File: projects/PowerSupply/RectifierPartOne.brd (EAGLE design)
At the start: 100 x 80 mm, 27 parts, among them K1 G2R2, K2 G2R2, X1 LINE-IN, X2 T1-PRI, X3 T1-SEC, X4 R1-OUT, X5 T2-PRI, X6 T2-SEC, X7 R2-OUT

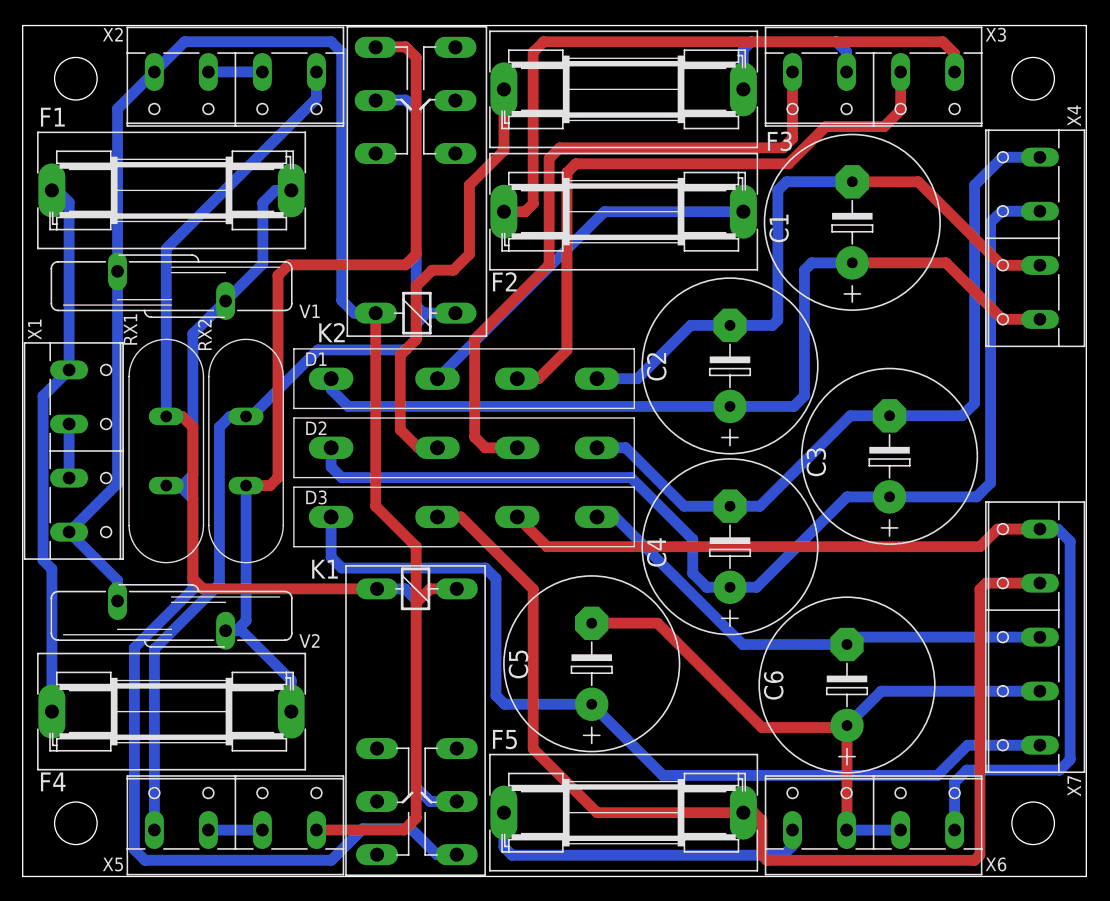
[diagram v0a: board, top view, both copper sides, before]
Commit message: feat: rectifier part modified
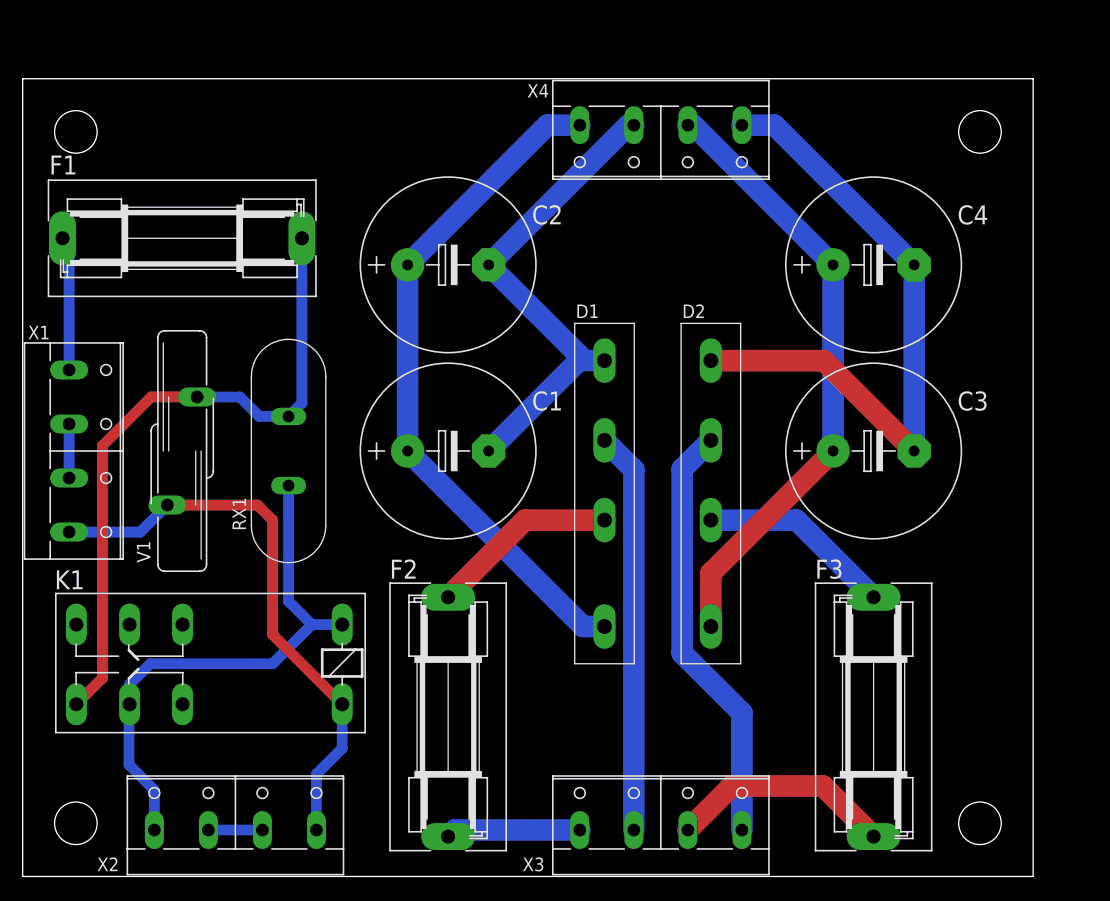
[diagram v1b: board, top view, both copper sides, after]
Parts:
- removed C5, C6: 2200µF, rcl:E7,5-16
- removed D3: B40C5000-3300A, bb84:B..C
- removed F4: 1.6AT, fuse:SH22,5A
- removed F5: 12AT, fuse:SH22,5A
- removed K2: G2R2, relay:G2R2
- removed RX2: B57364-S259, bb84:B57364S0
- removed V2: S20K230, varistor:S20K230
- removed X5: T2-PRI, con-wago-508:W237-4P
- removed X6: T2-SEC, con-wago-508:W237-4P
- removed X7: R2-OUT, con-wago-508:W237-5P
- moved X3 72.8 mm to (60.0, 5.00), turned to 0 degrees
- moved X2 70.0 mm to (20.0, 5.00), turned to 0 degrees
- moved F3 63.5 mm to (80.0, 15.0), turned to 90 degrees
- moved F2 50.3 mm to (40.0, 15.0), turned to 90 degrees
- moved D2 45.5 mm to (67.5, 20.0), turned to 90 degrees
- moved C1 43.7 mm to (40.0, 40.0), turned to 0 degrees
- moved D1 40.0 mm to (57.5, 20.0), turned to 90 degrees
- moved X4 36.4 mm to (60.0, 70.0), turned to 180 degrees
- moved C4 29.7 mm to (80.0, 57.5), turned to 0 degrees
- moved C2 28.2 mm to (40.0, 57.5), turned to 0 degrees
- moved V1 15.5 mm to (15.0, 40.0), turned to 0 degrees
- moved RX1 11.5 mm to (25.0, 40.0), turned to 90 degrees
- moved K1 10.5 mm to (27.5, 20.0), turned to 180 degrees
- moved F1 4.61 mm to (15.0, 60.0)
- moved C3 1.58 mm to (80.0, 40.0), turned to 0 degrees
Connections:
- removed net N$11: F4.2, K2.S1, RX2.P$2, V2.2
- removed net N$17: F5.1, X6.1
- removed net N$18: D3.VAC1, F5.2, X7.4
- removed net N$19: D3.VAC2, X6.4, X7.5
- removed net N$20: C5.+, D3.+VDC, X7.1
- removed net N$21: C6.-, D3.-VDC, X7.3
- removed net N$22: C5.-, C6.+, X6.2, X6.3, X7.2
- removed net N$23: X5.2, X5.3
- removed net N$24: K2.1, K2.P1, RX2.P$1, X5.1
- net +230VAC: no longer F4.1
- net -230VAC: no longer K2.2, V2.1, X5.4
- net N$4: now also X4.4; no longer X4.1
- net N$6: now also X4.2; no longer X4.3
- net N$7: now also X4.3; no longer X4.2
- net N$9: now also X4.1; no longer X4.4
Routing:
- net -230VAC: track 164.4 -> 53.6 mm
- net N$18: track 106.1 -> 0.00 mm
- net N$24: track 91.8 -> 0.00 mm
- net N$19: track 91.1 -> 0.00 mm
- net N$20: track 86.5 -> 0.00 mm
- net N$11: track 84.9 -> 0.00 mm
- net N$22: track 62.5 -> 0.00 mm
- net N$2: track 99.2 -> 51.0 mm
- net N$21: track 46.9 -> 0.00 mm
- net N$8: track 59.5 -> 12.6 mm
- net N$6: track 104.0 -> 57.9 mm
- net N$3: track 105.6 -> 62.8 mm
- net +230VAC: track 51.3 -> 12.6 mm
- net N$17: track 32.5 -> 0.00 mm
- net N$15: track 63.4 -> 40.1 mm
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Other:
- board size 100 x 80 mm -> 95 x 75 mm

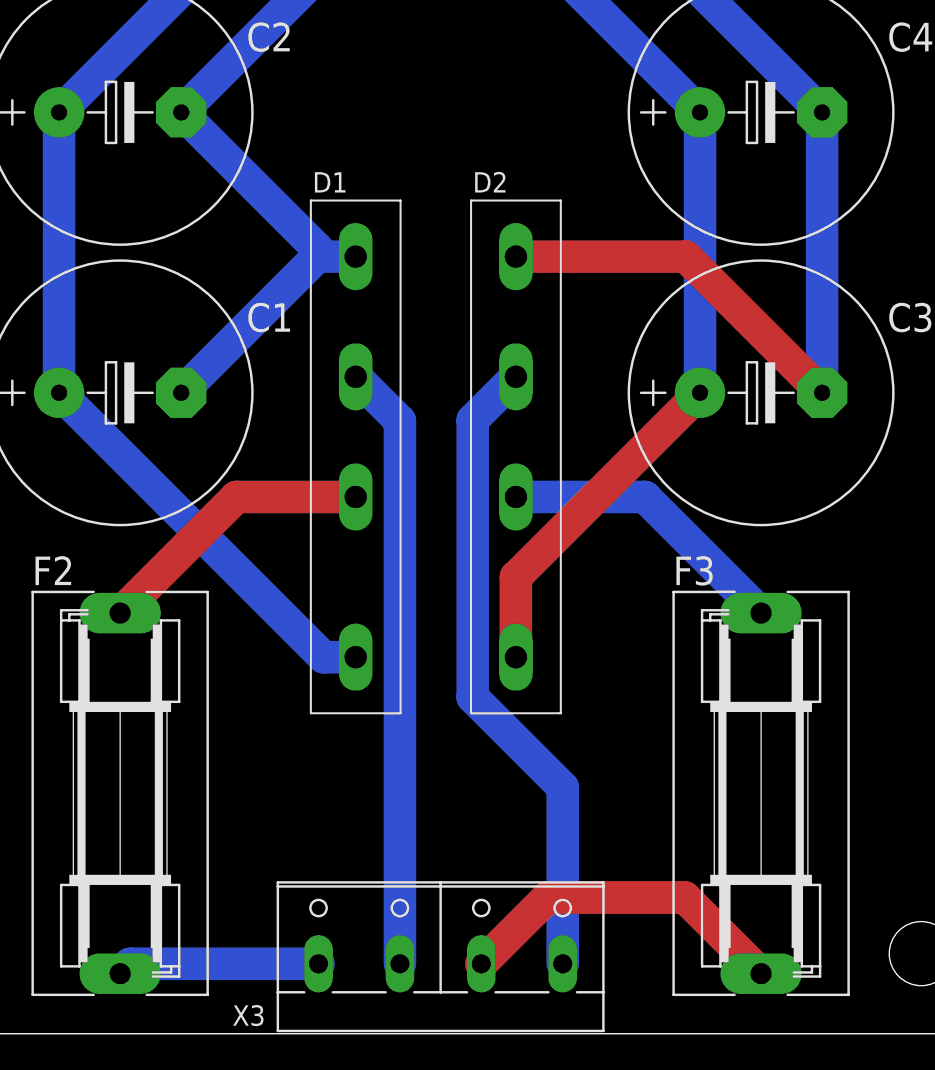
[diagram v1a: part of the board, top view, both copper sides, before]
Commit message: feat: rectifier part one modified
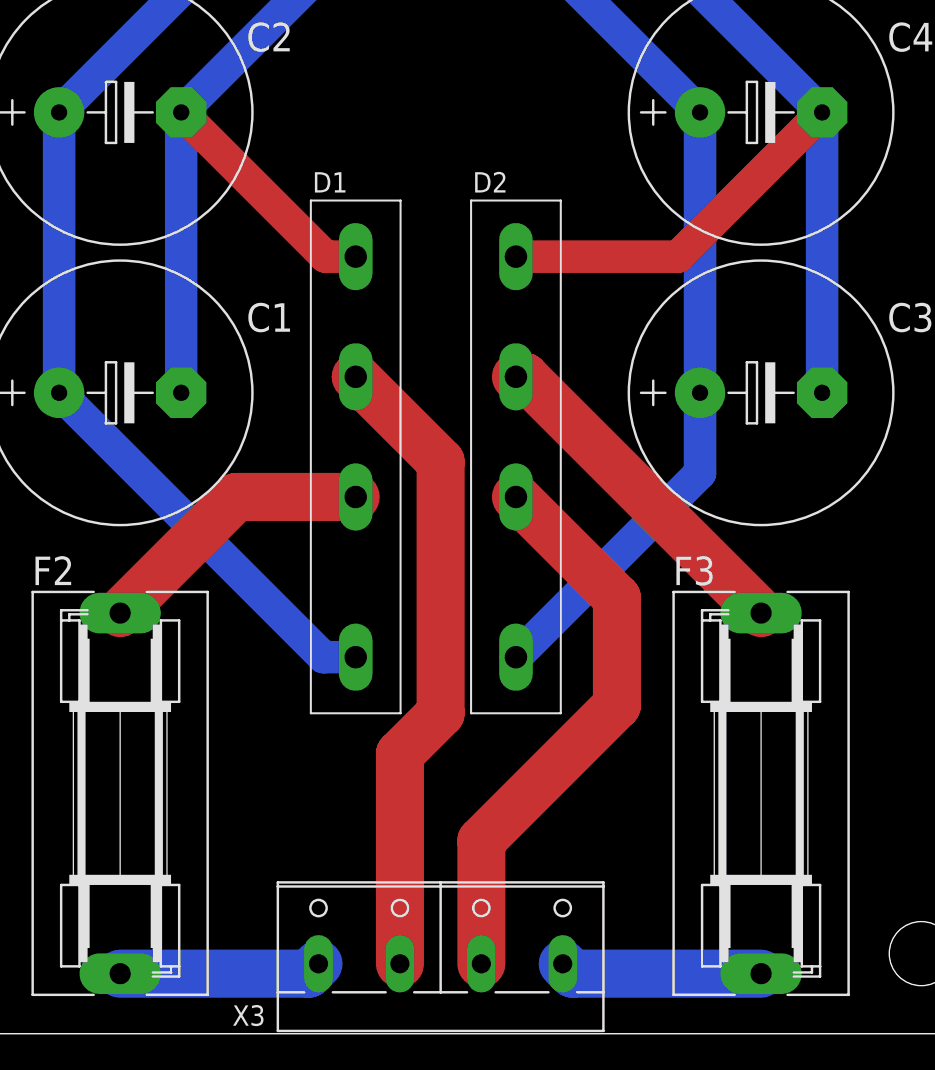
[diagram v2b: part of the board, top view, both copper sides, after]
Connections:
- removed net N$13: F3.1, X3.3
- removed net N$15: D2.VAC2, X3.4
- new net N$11: D2.VAC2, F3.2
- new net N$12: F3.1, X3.4
- net N$14: now also X3.3; no longer F3.2
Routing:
- net N$15: track 40.1 -> 0.00 mm
- net N$11: track 0.00 -> 21.4 mm
- net N$13: track 21.1 -> 0.00 mm
- net N$14: track 18.3 -> 35.2 mm
- net N$12: track 0.00 -> 12.6 mm
- net N$7: track 46.0 -> 51.2 mm
- net N$1: track 37.8 -> 39.9 mm
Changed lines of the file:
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@@
 <contactref element="C1" pad="+"/>
 <contactref element="X4" pad="4"/>
-<wire x1="36.19" y1="57.5" x2="49.325" y2="70.635" width="2.032" layer="16"/>
-<wire x1="49.325" y1="70.635" x2="52.38" y2="70.635" width="2.032" layer="16"/>
 <wire x1="54.7" y1="23.5" x2="52.69" y2="23.5" width="2.032" layer="16"/>
 <wire x1="52.69" y1="23.5" x2="36.19" y2="40" width="2.032" layer="16"/>
 <wire x1="36.19" y1="40" x2="36.19" y2="57.5" width="2.032" layer="16"/>
+<wire x1="36.19" y1="57.5" x2="49.325" y2="70.635" width="2.032" layer="16"/>
+<wire x1="49.325" y1="70.635" x2="52.38" y2="70.635" width="2.032" layer="16"/>
 </signal>
 <signal name="N$6">
@@
 <wire x1="76.19" y1="57.5" x2="63.055" y2="70.635" width="2.032" layer="16"/>
 <wire x1="63.055" y1="70.635" x2="62.54" y2="70.635" width="2.032" layer="16"/>
-<wire x1="64.7" y1="23.5" x2="64.7" y2="28.51" width="2.032" layer="1"/>
-<wire x1="64.7" y1="28.51" x2="76.19" y2="40" width="2.032" layer="1"/>
+<wire x1="76.19" y1="40" x2="76.19" y2="34.99" width="2.032" layer="16"/>
+<wire x1="76.19" y1="34.99" x2="64.7" y2="23.5" width="2.032" layer="16"/>
 </signal>
 <signal name="N$7">
@@
 <contactref element="C2" pad="-"/>
 <contactref element="X4" pad="3"/>
-<wire x1="43.81" y1="40" x2="52.31" y2="48.5" width="2.032" layer="16"/>
-<wire x1="52.31" y1="48.5" x2="54.7" y2="48.5" width="2.032" layer="16"/>
-<wire x1="52.31" y1="48.5" x2="52.31" y2="49" width="2.032" layer="16"/>
-<wire x1="52.31" y1="49" x2="43.81" y2="57.5" width="2.032" layer="16"/>
 <wire x1="43.81" y1="57.5" x2="56.945" y2="70.635" width="2.032" layer="16"/>
 <wire x1="56.945" y1="70.635" x2="57.46" y2="70.635" width="2.032" layer="16"/>
+<wire x1="43.81" y1="57.5" x2="43.81" y2="40" width="2.032" layer="16"/>
+<wire x1="54.7" y1="48.5" x2="52.81" y2="48.5" width="2.032" layer="1"/>
+<wire x1="52.81" y1="48.5" x2="43.81" y2="57.5" width="2.032" layer="1"/>
 </signal>
 <signal name="N$9">
@@
 <wire x1="70.675" y1="70.635" x2="67.62" y2="70.635" width="2.032" layer="16"/>
 <wire x1="83.81" y1="57.5" x2="83.81" y2="40" width="2.032" layer="16"/>
-<wire x1="64.7" y1="48.5" x2="75.31" y2="48.5" width="2.032" layer="1"/>
-<wire x1="75.31" y1="48.5" x2="83.81" y2="40" width="2.032" layer="1"/>
+<wire x1="64.7" y1="48.5" x2="74.81" y2="48.5" width="2.032" layer="1"/>
+<wire x1="74.81" y1="48.5" x2="83.81" y2="57.5" width="2.032" layer="1"/>
 </signal>
 <signal name="PE">
@@
 <contactref element="D1" pad="VAC2"/>
 <contactref element="X3" pad="2"/>
-<wire x1="57.46" y1="4.365" x2="57.46" y2="38.24" width="2.032" layer="16"/>
-<wire x1="57.46" y1="38.24" x2="54.7" y2="41" width="2.032" layer="16"/>
+<wire x1="57.46" y1="4.365" x2="57.46" y2="17.46" width="3" layer="1"/>
+<wire x1="57.46" y1="17.46" x2="60" y2="20" width="3" layer="1"/>
+<wire x1="60" y1="20" x2="60" y2="35.7" width="3" layer="1"/>
+<wire x1="60" y1="35.7" x2="54.7" y2="41" width="3" layer="1"/>
 </signal>
 <signal name="N$8">
 <contactref element="X3" pad="1"/>
 <contactref element="F2" pad="1"/>
-<wire x1="52.38" y1="4.365" x2="40.6172" y2="4.365" width="2.032" layer="16"/>
-<wire x1="40.6172" y1="4.365" x2="40" y2="3.7478" width="2.032" layer="16"/>
+<wire x1="40" y1="3.7478" x2="51.7628" y2="3.7478" width="3" layer="16"/>
+<wire x1="51.7628" y1="3.7478" x2="52.38" y2="4.365" width="3" layer="16"/>
 </signal>
 <signal name="N$10">
 <contactref element="F2" pad="2"/>
 <contactref element="D1" pad="VAC1"/>
-<wire x1="40" y1="26.2522" x2="47.2478" y2="33.5" width="2.032" layer="1"/>
-<wire x1="47.2478" y1="33.5" x2="54.7" y2="33.5" width="2.032" layer="1"/>
-</signal>
-<signal name="N$13">
-<contactref element="X3" pad="3"/>
-<contactref element="F3" pad="1"/>
-<wire x1="62.54" y1="4.365" x2="66.675" y2="8.5" width="2.032" layer="1"/>
-<wire x1="75.2478" y1="8.5" x2="80" y2="3.7478" width="2.032" layer="1"/>
-<wire x1="66.675" y1="8.5" x2="75.2478" y2="8.5" width="2.032" layer="1"/>
+<wire x1="40" y1="26.2522" x2="47.2478" y2="33.5" width="3" layer="1"/>
+<wire x1="47.2478" y1="33.5" x2="54.7" y2="33.5" width="3" layer="1"/>
 </signal>
 <signal name="N$14">
 <contactref element="D2" pad="VAC1"/>
-<contactref element="F3" pad="2"/>
-<wire x1="64.7" y1="33.5" x2="72.7522" y2="33.5" width="2.032" layer="16"/>
-<wire x1="72.7522" y1="33.5" x2="80" y2="26.2522" width="2.032" layer="16"/>
-</signal>
-<signal name="N$15">
-<contactref element="D2" pad="VAC2"/>
-<contactref element="X3" pad="4"/>
-<wire x1="67.62" y1="4.365" x2="67.62" y2="15.38" width="2.032" layer="16"/>
-<wire x1="67.62" y1="15.38" x2="62" y2="21" width="2.032" layer="16"/>
-<wire x1="62" y1="21" x2="62" y2="38.3" width="2.032" layer="16"/>
-<wire x1="62" y1="38.3" x2="64.7" y2="41" width="2.032" layer="16"/>
+<contactref element="X3" pad="3"/>
+<wire x1="62.54" y1="4.365" x2="62.54" y2="12.04" width="3" layer="1"/>
+<wire x1="62.54" y1="12.04" x2="71" y2="20.5" width="3" layer="1"/>
+<wire x1="71" y1="20.5" x2="71" y2="27.2" width="3" layer="1"/>
+<wire x1="71" y1="27.2" x2="64.7" y2="33.5" width="3" layer="1"/>
 </signal>
 <signal name="+230VAC">
@@
 <wire x1="25" y1="25.866" x2="25" y2="36.75" width="1.016" layer="16"/>
 </signal>
+<signal name="N$12">
+<contactref element="F3" pad="1"/>
+<contactref element="X3" pad="4"/>
+<wire x1="80" y1="3.7478" x2="68.2372" y2="3.7478" width="3" layer="16"/>
+<wire x1="68.2372" y1="3.7478" x2="67.62" y2="4.365" width="3" layer="16"/>
+</signal>
+<signal name="N$11">
+<contactref element="F3" pad="2"/>
+<contactref element="D2" pad="VAC2"/>
+<wire x1="80" y1="26.2522" x2="65.2522" y2="41" width="3" layer="1"/>
+<wire x1="65.2522" y1="41" x2="64.7" y2="41" width="3" layer="1"/>
+</signal>
 </signals>
